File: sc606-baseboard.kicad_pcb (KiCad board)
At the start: 6 copper layers, 100 x 80 mm, 459 parts, among them IC1 TPS54561DPRT, IC2 TPS7A0518PDBVT, IC3 TPS7A0518PDBVT, J1 PJ-202A, J10 E8124-015-01, J11 E8124-015-01, J12 E8124-015-01, J14 CONMMCX002-SMD-T, J2 WE_68715014522, J3 F52R-1A7H1-11020, J4 46756-1001, J5 U_FL-R-SMT-1_10_, J6 E8124-015-01, J7 DM3AT-SF-PEJM5, J8 693022010811, J9 E8124-015-01, M1 SC606T, Q1 BSS138APW, Q10 BSS84, Q11 Si7223DN, Q2 BSS138-7-F, Q3 BSS138APW, Q4 BSS138APW, Q5 BSS138APW, Q6 BSS138APW, Q7 BSS138-7-F, Q8 BSS138-7-F, Q9 SQS401EN-T1_BE3, SW1 1X03, U1 AP62301WU-7, U10 NCP163ASN330T1G, U11 EMIF06-MSD02N16, U12 STUSB4500QTR, U13 FT232RQ-REEL, U14 LTC4416IMS-1, U15 USB57442G, U2 AP62301WU-7, U3 AP62301WU-7, U4 74LVC1G123GN, U5 NTS0102GT, U6 PCA9547BS, U7 LT9611UXC, U8 NTS0102GT, U9 FSUSB30UMX, Y1 ABM8G-24.000MHZ-18-D2Y-T, Y2 ABM8G-25.000MHZ-B4Y-T

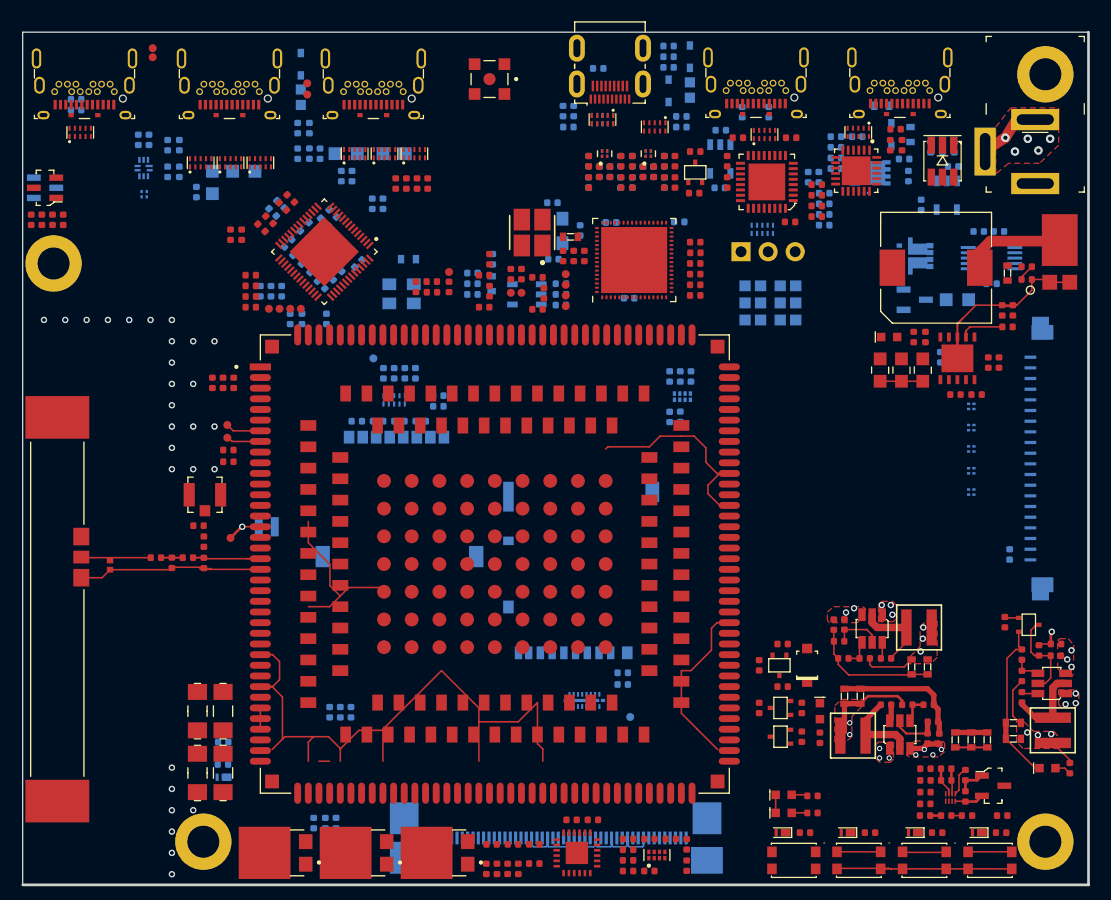
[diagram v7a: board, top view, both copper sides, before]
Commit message: Changed barrel jack model, added power path controller
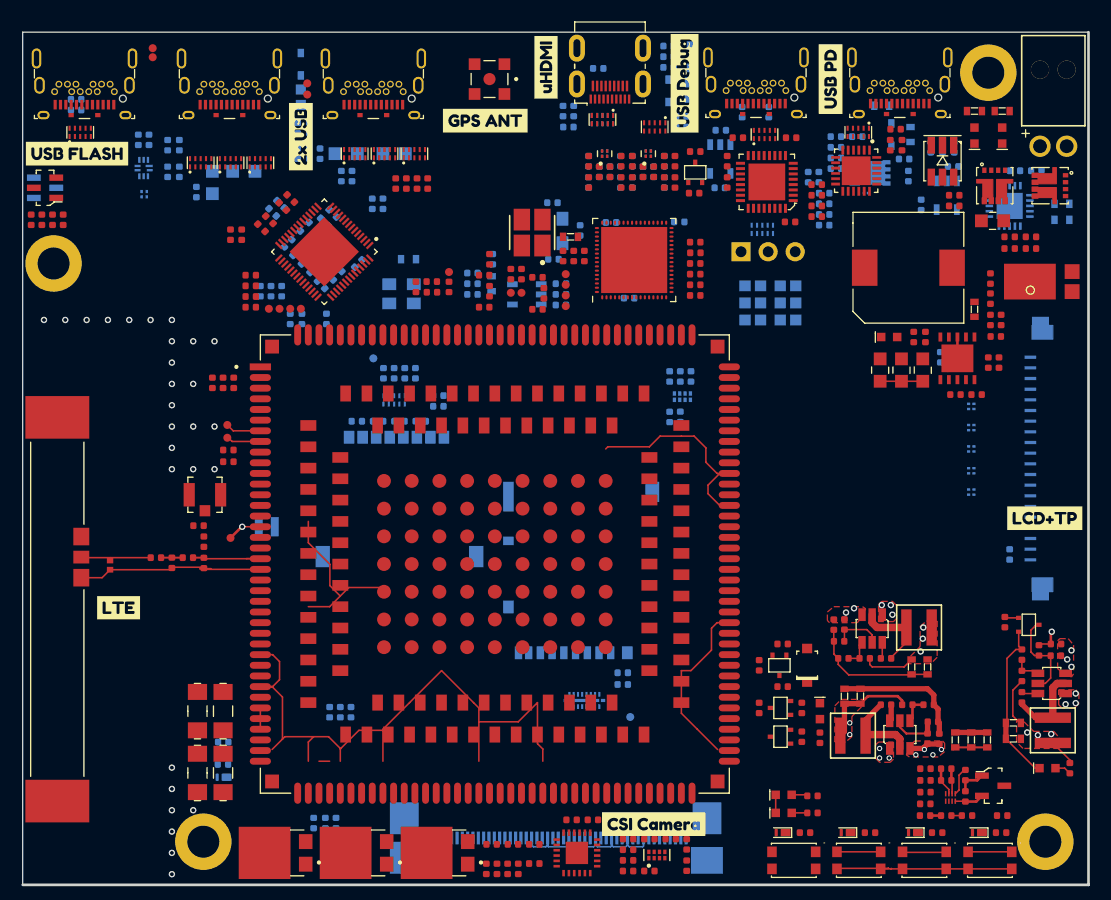
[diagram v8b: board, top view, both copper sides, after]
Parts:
- added C156: C_100n_0402, antmicro-footprints:0402-cap, F.Cu at (163.0, 57.7)
- added C157: C_100n_0402, antmicro-footprints:0402-cap, F.Cu at (163.0, 58.7)
- added C158: C_1n_0402, antmicro-footprints:0402-res, B.Cu at (170.7, 55.4)
- added C159: C_100n_0402, antmicro-footprints:0402-cap, B.Cu at (168.7, 55.4)
- added D36: KP-1608EC, sc606-baseboard-footprints:LED_0603, F.Cu at (167.5, 52.1)
- added D37: KP-1608EC, sc606-baseboard-footprints:LED_0603, F.Cu at (164.9, 52.1)
- added R165: R_768k_0402, antmicro-footprints:0402-res, F.Cu at (168.2, 62.7)
- added R166: R_97k6_0402, antmicro-footprints:0402-res, F.Cu at (170.2, 62.7)
- added R167: R_30k1_0603, antmicro-footprints:0603-res, B.Cu at (173.1, 60.0)
- added R168: R_270R_0603, antmicro-footprints:0603-res, F.Cu at (167.5, 49.8)
- added R169: R_270R_0603, antmicro-footprints:0603-res, F.Cu at (164.9, 49.8)
- added kibuzzard-6200CC83: G***, label, F.Cu at (134.8, 116.7)
- added kibuzzard-6200CC9F: G***, label, F.Cu at (84.6, 96.4)
- added kibuzzard-6200CCB6: G***, label, F.Cu at (171.5, 88.0)
- added kibuzzard-6200CCD6: G***, label, F.Cu at (80.7, 53.8)
- added kibuzzard-6200CCE7: G***, label, F.Cu at (101.7, 52.2)
- added kibuzzard-6200CD20: G***, label, F.Cu at (124.7, 45.7)
- added kibuzzard-6200CD3C: G***, label, F.Cu at (137.7, 47.2)
- added kibuzzard-6200CD90: G***, label, F.Cu at (119.0, 50.7)
- added kibuzzard-6200CDB4: G***, label, F.Cu at (151.4, 46.8)
- C153: footprint antmicro-footprints:0805-cap -> sc606-baseboard-footprints:0805-cap; moved to F.Cu
- J1: value PJ-202A -> 1053131102; footprint sc606-baseboard-footprints:Barrel_Jack_5.5mmODx2.1mmID_PJ-202A -> antmicro-footprints:1053131102
- Q10: value BSS84 -> Si7223DN; footprint antmicro-footprints:SOT-23-3 -> sc606-baseboard-footprints:PowerPak-1212; moved to F.Cu
- Q11: footprint sa800u-baseboard-hw-footprints:PowerPak-1212 -> sc606-baseboard-footprints:PowerPak-1212; moved to F.Cu
- R161: value R_220k_0402 -> R_768k_0402; moved to F.Cu
- R163: value R_24k9_0402 -> R_97k6_0402; moved to F.Cu
- R164: value R_180k_0402 -> R_30k1_0603; footprint antmicro-footprints:0402-res -> antmicro-footprints:0603-res
- U14: value LTC4416IMS-1 -> LTC4418IUF#PBF; footprint antmicro-footprints:MSOP-10_MS -> antmicro-footprints:QFN-20_1EP_4x4_P0.5mm
- moved Q11 14.3 mm to (172.0, 56.8), turned to 0 degrees
- moved Q10 13.1 mm to (166.8, 56.8), turned to 90 degrees
- moved C153 8.10 mm to (166.6, 60.1), turned to 180 degrees
- moved R164 6.45 mm to (173.1, 58.5), turned to 180 degrees
- moved MP1 5.35 mm to (166.2, 46.2)
- moved U14 5.19 mm to (168.2, 58.7)
- moved R163 4.93 mm to (170.2, 61.6)
- moved R161 4.72 mm to (168.2, 61.6), turned to 180 degrees
- moved R13 4.60 mm to (164.9, 68.4)
- moved D2 4.08 mm to (170.6, 65.7), turned to 0 degrees
- moved R15 3.85 mm to (166.4, 67.4), turned to 270 degrees
- moved R14 3.58 mm to (166.4, 65.5), turned to 270 degrees
- moved L2 2.60 mm to (158.7, 64.5)
- moved J1 1.77 mm to (172.3, 53.1), turned to 180 degrees
- moved C22 1.42 mm to (167.4, 69.4)
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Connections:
- Q10 pad 1: Net-(Q10-Pad1) -> Net-(C157-Pad2)
- Q10 pad 2: PD_VDD -> Net-(Q10-Pad2)
- Q10 pad 3: VDD -> Net-(C157-Pad2)
- Q11 pad 1: Net-(Q11-Pad1) -> Net-(C156-Pad2)
- Q11 pad 3: Net-(Q11-Pad1) -> Net-(C156-Pad2)
- Q11 pad 5: VDD -> (no net)
- R161 pad 1: AUX_VDD -> Net-(R161-Pad1)
- R161 pad 2: Net-(R161-Pad2) -> AUX_VDD
- R163 pad 1: GND -> Net-(R161-Pad1)
- R163 pad 2: Net-(R161-Pad2) -> Net-(R163-Pad2)
- R164 pad 1: Net-(R161-Pad2) -> GND
- R164 pad 2: Net-(R164-Pad2) -> Net-(R163-Pad2)
- U14 pad 1: Net-(R164-Pad2) -> Net-(C158-Pad1)
- U14 pad 10: Net-(Q11-Pad2) -> Net-(C159-Pad2)
- U14 pad 2: Net-(R161-Pad2) -> Net-(R161-Pad1)
- U14 pad 3: GND -> Net-(R163-Pad2)
- U14 pad 4: GND -> Net-(R165-Pad1)
- U14 pad 5: (no net) -> Net-(R166-Pad2)
- U14 pad 6: Net-(Q10-Pad1) -> Net-(D36-Pad2)
- U14 pad 7: PD_VDD -> Net-(D37-Pad2)
- U14 pad 8: VDD -> GND
- U14 pad 9: AUX_VDD -> (no net)
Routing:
- net GND: track 239.3 -> 219.1 mm, vias 37 -> 32
- net Net-(C25-Pad2): track 9.53 -> 0.00 mm
- net Net-(C23-Pad1): track 4.17 -> 0.00 mm
- net Net-(IC1-Pad6): track 1.60 -> 0.00 mm
